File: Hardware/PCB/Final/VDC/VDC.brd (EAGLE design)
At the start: 97.5 x 80 mm, 80 parts, among them U1 IL300, U10 IL300, U11 MCP602-E/P, U12 MCP602-E/P, U13 AD7993BRUZ-0, U2 MCP602-E/P, U3 MCP602-E/P, U4 IL300, U5 MCP602-E/P, U6 MCP602-E/P, U7 IL300, U8 MCP602-E/P, U9 MCP602-E/P

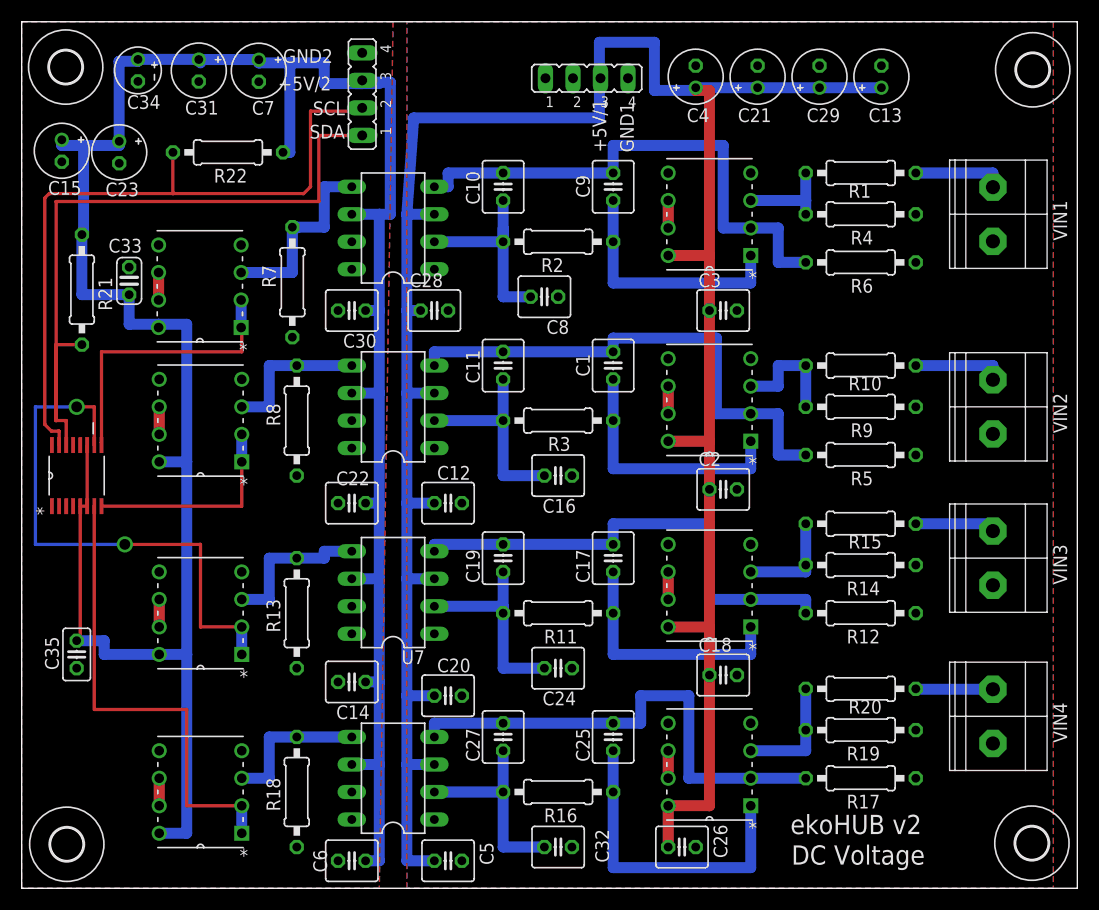
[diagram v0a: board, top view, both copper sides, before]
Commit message: Made changes to the PCB Folders
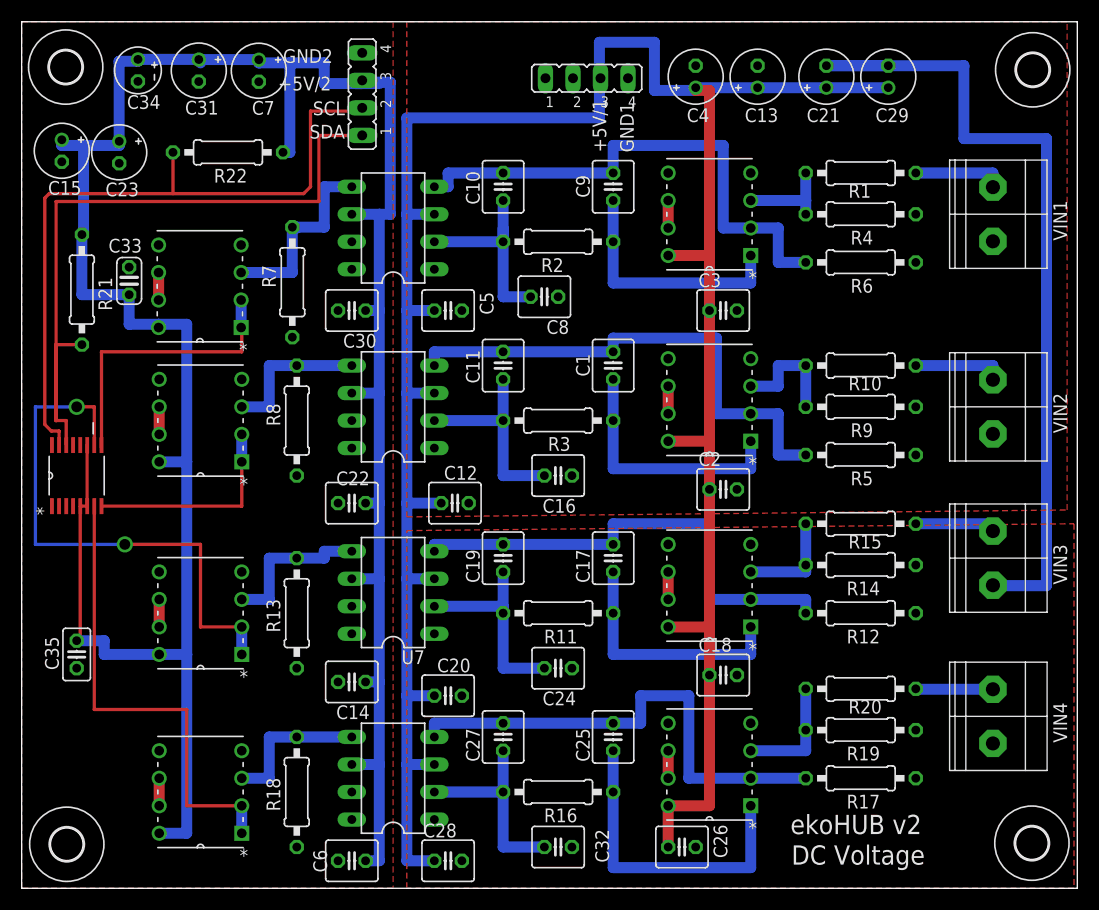
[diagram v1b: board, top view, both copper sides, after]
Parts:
- moved C28 50.8 mm to (39.4, 2.54)
- moved C5 50.8 mm to (39.4, 53.3)
- moved C13 11.4 mm to (67.9, 74.9)
- moved C21 6.35 mm to (74.3, 74.9)
- moved C29 6.35 mm to (80.0, 74.9)
- moved C12 0.64 mm to (40.0, 35.6)
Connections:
- new net PE: C18.2, C20.2, C21.-, C24.1, C26.2, C28.2, C29.-, C32.1, R12.1, R14.1, R17.1, R19.1, U10.1, U11.4, U11.5, U7.1, U8.4, U8.5, VIN3.P$1, VIN4.P$1
- net GND1: no longer C18.2, C20.2, C21.-, C24.1, C26.2, C28.2, C29.-, C32.1, R12.1, R14.1, R17.1, R19.1, U10.1, U11.4, U11.5, U7.1, U8.4, U8.5, VIN3.P$1, VIN4.P$1
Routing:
- net PE: track 0.00 -> 79.0 mm
- net +5V/1: track 230.4 -> 233.5 mm
- added copper zone on layer 1, net PE
- removed copper zone on layer 16, net N$23
- removed copper zone on layer 16, net N$24
